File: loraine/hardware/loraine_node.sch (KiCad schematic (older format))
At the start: 37 parts, among them CON1 BARREL_JACK, IC1 ATTINY2313A-S, K1 CONN_GND, K2 CONN_LEDS, K3 CONN_12V, P1 POWER_THRU, P2 POWER, P3 SOLDER_PAD, P4 ICSP, P5 OUTPUTS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

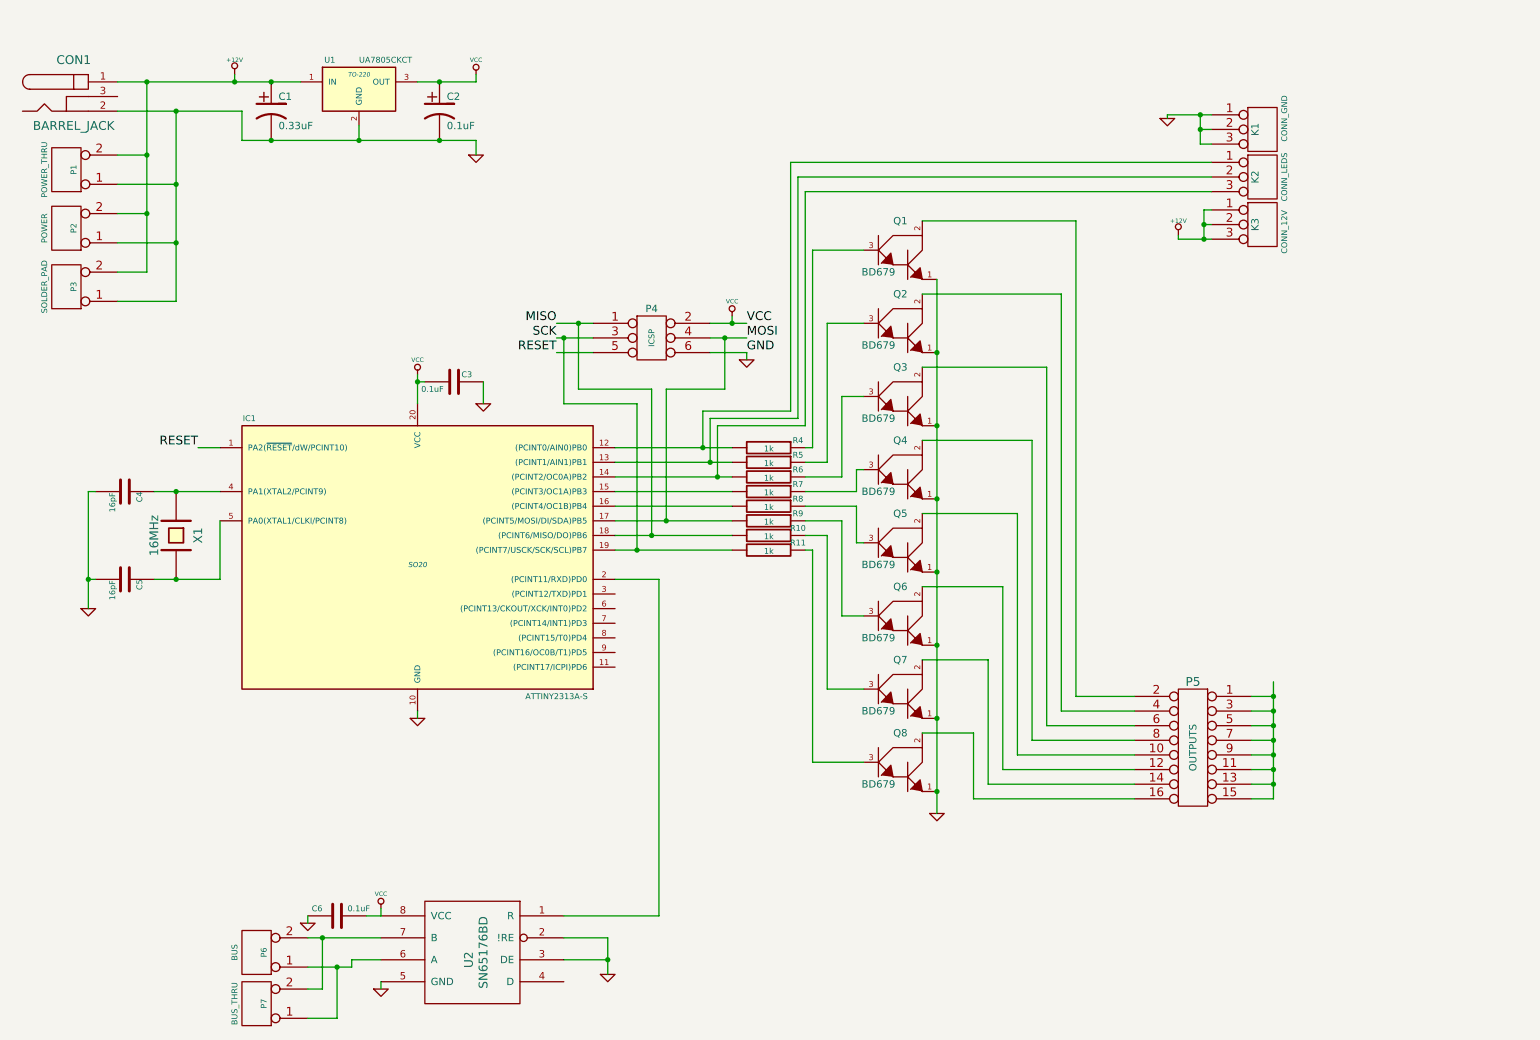
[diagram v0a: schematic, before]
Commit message: Proposed design: 1 board 3x3 RGB LEDs
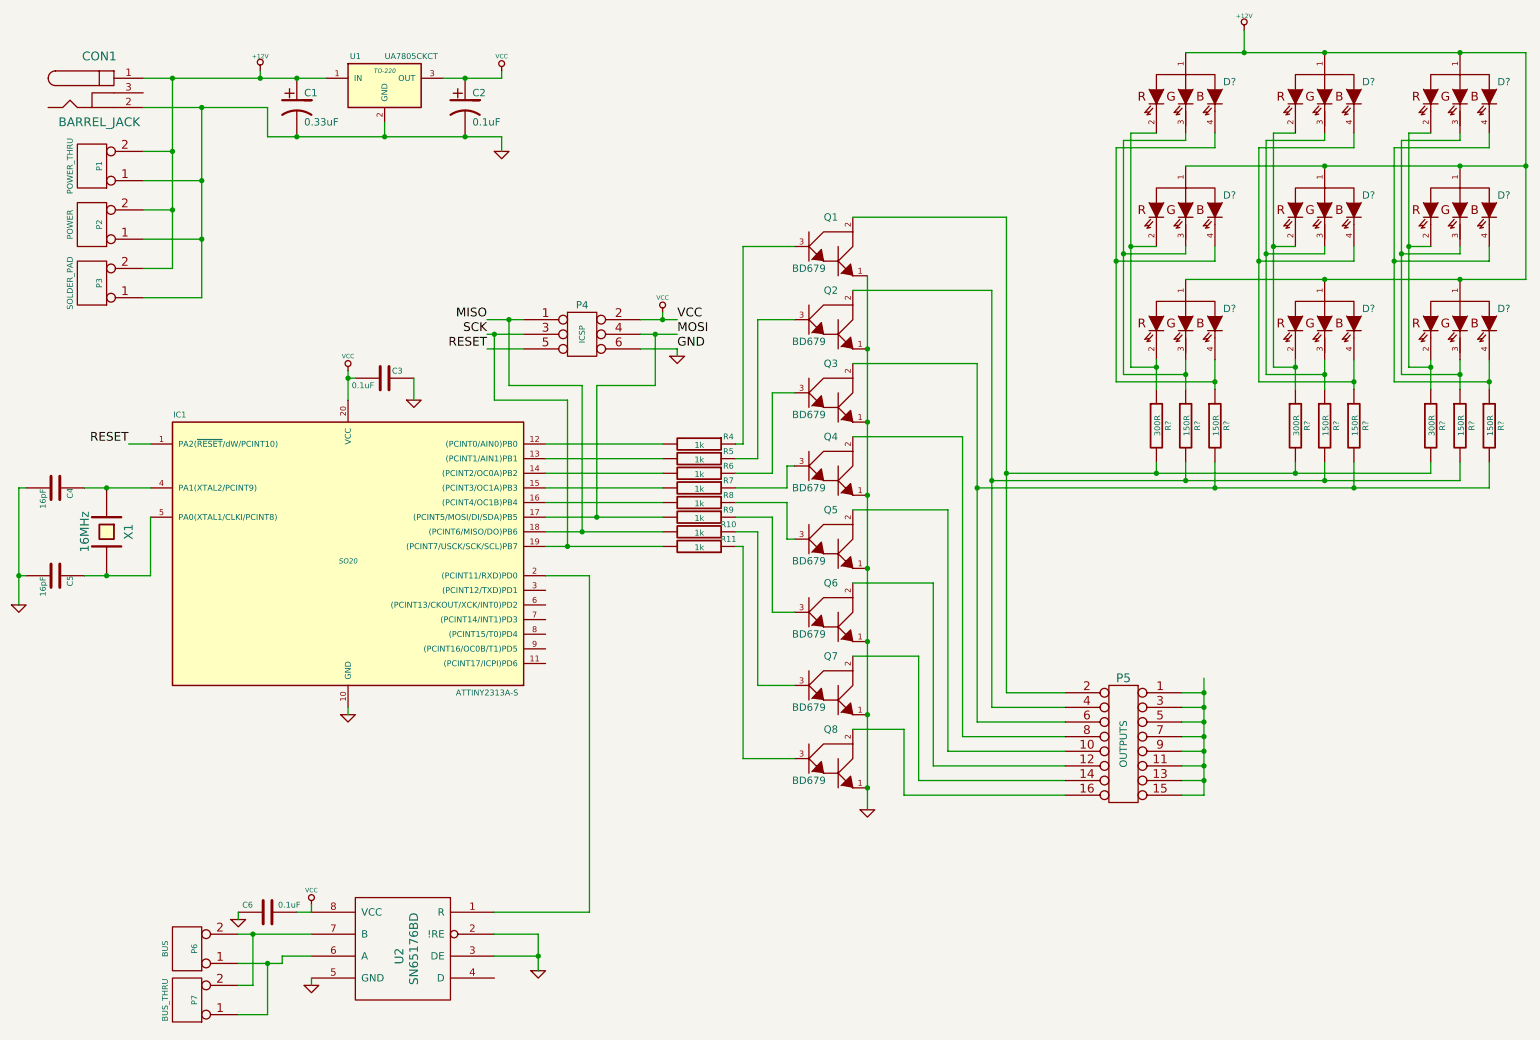
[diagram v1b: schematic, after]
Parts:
- removed K1: CONN_GND, symbol CONN_3
- removed K2: CONN_LEDS, symbol CONN_3
- removed K3: CONN_12V, symbol CONN_3
- added D? (x9): RGB_LED, symbol RGB_LED
- added R? (x3): 300R, symbol R
- added R? (x6): 150R, symbol R
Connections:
- net +12V: now also D?.1 (A), D?.1 (A), D?.1 (A), D?.1 (A), D?.1 (A), D?.1 (A), D?.1 (A), D?.1 (A), D?.1 (A)
- net at P5.2, Q1.2: now also R?.2, R?.2, R?.2
- net at P5.4, Q2.2: now also R?.2, R?.2, R?.2
- net at P5.6, Q3.2: now also R?.2, R?.2, R?.2
- new net: D?.2 (RED), D?.2 (RED), D?.2 (RED), R?.1 (x3)
- new net: D?.3 (BLUE), D?.3 (BLUE), D?.3 (BLUE), R?.1 (x3)
- new net: D?.4 (GREEN), D?.4 (GREEN), D?.4 (GREEN), R?.1 (x3)
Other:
- moved on the sheet: C1, C2, C3, C4, C5, C6, CON1, IC1, P1, P2, P3, P4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
